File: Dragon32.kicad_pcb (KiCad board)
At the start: 2 copper layers, 120.2 x 78.9 mm, 59 parts, among them IC1 74LS273N, IC10 74LS32N, IC11 74LS123N, IC12 LM1889N, IC13 2318, IC15 MC14053, IC2 MC6847, IC3 74LS00N, IC4 74LS20N, IC5 74LS86AN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

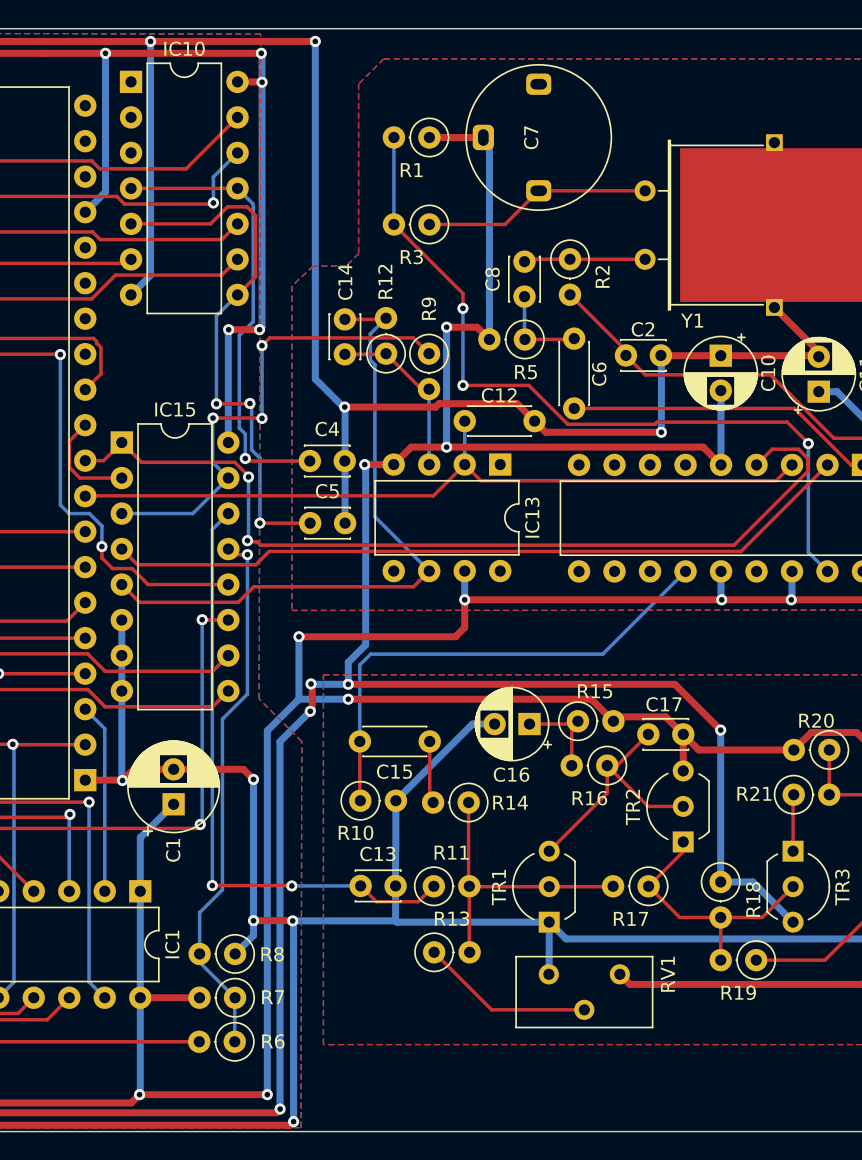
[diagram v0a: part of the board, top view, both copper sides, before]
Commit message: fix diff amp wiring
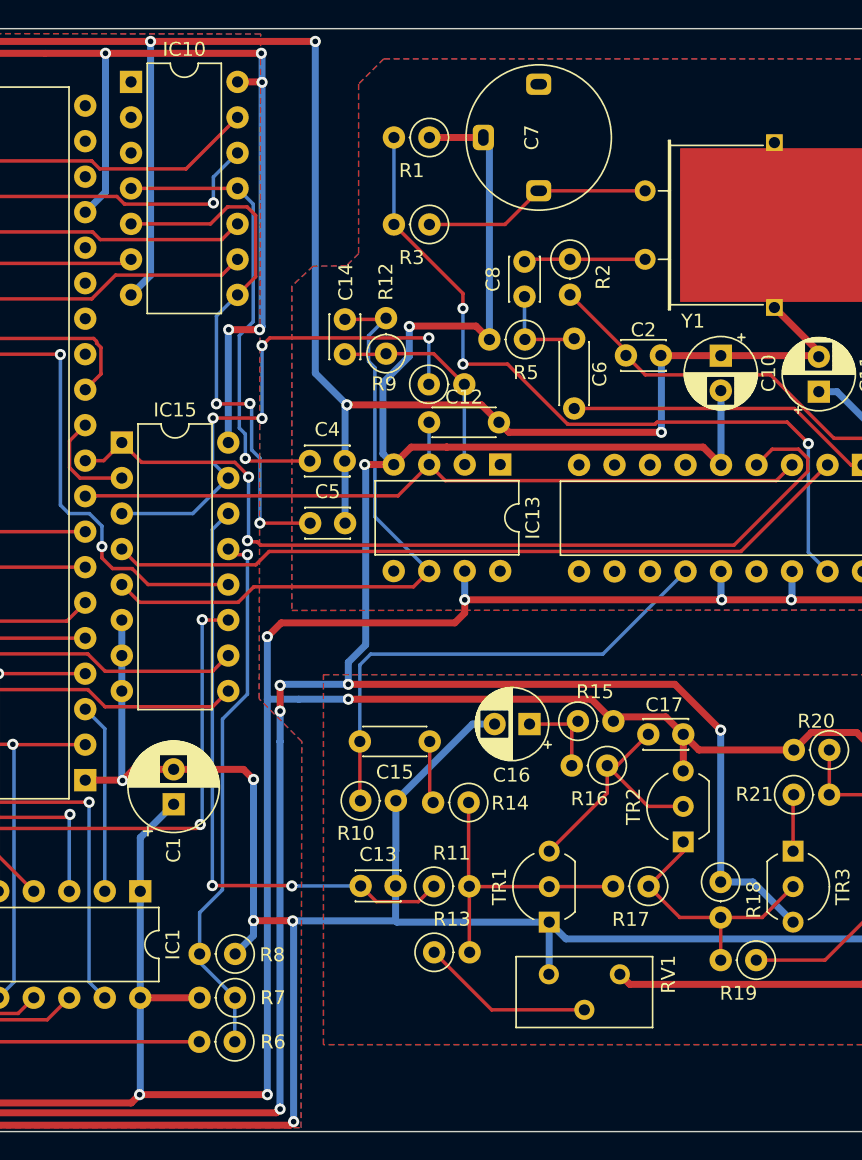
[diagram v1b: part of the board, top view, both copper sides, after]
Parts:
- moved C12 2.55 mm to (317.1, 78.5)
- moved R9 2.20 mm to (317.1, 75.7), turned to 0 degrees
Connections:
- C14 pad 1: Net-(IC13-+) -> Net-(IC13--)
- IC13 pad 2: CHB -> Net-(IC13--)
- IC13 pad 3: Net-(IC13-+) -> CHB
- R12 pad 1: Net-(IC13-+) -> Net-(IC13--)
- R9 pad 2: Net-(IC13-+) -> Net-(IC13--)
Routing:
- net Net-(IC13--): track 0.00 -> 15.2 mm
- net Net-(IC13-+): track 12.5 -> 0.00 mm
- net -5V: track 261.8 -> 268.1 mm, vias 10 -> 9
- net +5V: track 592.7 -> 595.6 mm
- net MUX Y: track 34.8 -> 37.7 mm, vias 3 -> 4
- net ChrOSC: track 56.1 -> 55.2 mm

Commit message: notch edge of board for clearance of relay
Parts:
- moved R20 138.4 mm to (207.6, 110.1), turned to 90 degrees
- moved R1 137.3 mm to (180.0, 64.8)
- moved C7 137.3 mm to (187.9, 64.8)
- moved R3 137.2 mm to (180.0, 68.6)
- moved C16 136.5 mm to (187.9, 105.7), turned to -90 degrees
- moved R13 135.4 mm to (182.6, 127.7)
- moved R19 135.3 mm to (205.6, 127.3)
- moved R14 135.2 mm to (185.0, 114.8)
- moved C15 135.2 mm to (182.2, 110.5)
- moved R10 135.2 mm to (177.3, 114.7)
- moved R18 135.2 mm to (203.0, 120.2)
- moved TR3 135.2 mm to (208.2, 118.0)
- moved R17 135.2 mm to (197.9, 120.5)
- moved RV1 135.2 mm to (195.9, 127.4)
- moved C17 135.1 mm to (200.4, 108.4)
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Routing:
- net GND: track 642.0 -> 572.8 mm
- net +5V: track 595.6 -> 609.4 mm
- net MUX Y: track 37.7 -> 43.1 mm
- net Net-(TR1-C): track 18.4 -> 23.4 mm
- net VID OUT: track 10.8 -> 15.6 mm
- net Composite: track 35.8 -> 40.0 mm
- net Net-(TR2-E): track 19.4 -> 22.6 mm
- net MUX X: track 43.9 -> 46.4 mm
- net Net-(TR3-E): track 4.06 -> 6.37 mm
- net Net-(C16-Pad1): track 6.91 -> 8.99 mm
- net Net-(TR1-B): track 21.1 -> 23.1 mm
- net Net-(C7-Pad1): track 16.4 -> 18.1 mm
- net -5V: track 268.1 -> 268.9 mm
- net Net-(R13-Pad1): track 12.5 -> 11.7 mm
- net GM2: track 90.5 -> 89.8 mm
- removed copper zone on B.Cu, net (none)
- removed copper zone on F.Cu, net (none)
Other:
- outline, holes or cut-outs redrawn

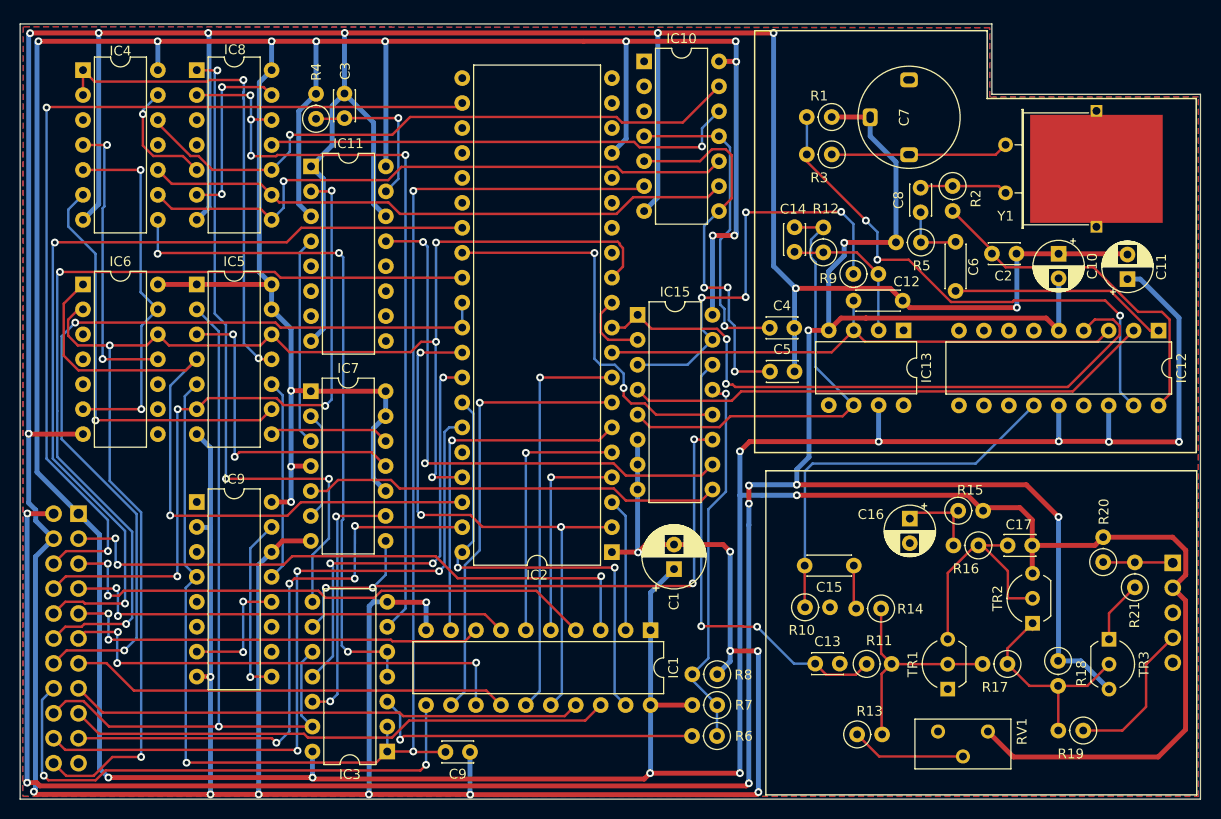
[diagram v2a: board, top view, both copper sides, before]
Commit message: move -5v
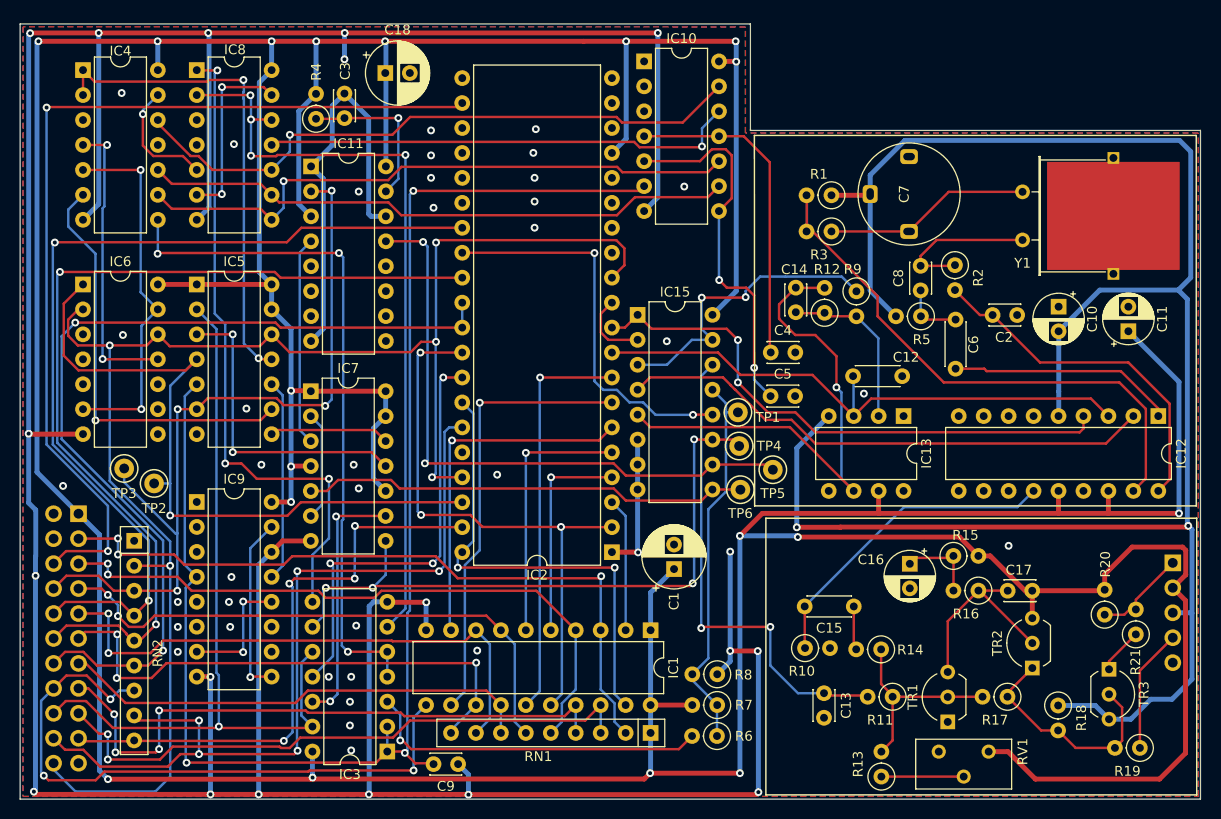
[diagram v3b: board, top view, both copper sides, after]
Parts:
- added C18: 100uF, Capacitor_THT:CP_Radial_D6.3mm_P2.50mm, F.Cu at (134.5, 60.3)
- added RN1: 4K7, Resistor_THT:R_Array_SIP9, F.Cu at (161.5, 127.5)
- added RN2: 4K7, Resistor_THT:R_Array_SIP9, F.Cu at (109.0, 108.0)
- added TP1: TestPoint_LinePulse, TestPoint:TestPoint_Keystone_5000-5004_Miniature, F.Cu at (170.4, 94.9)
- added TP2: TestPoint_HS, TestPoint:TestPoint_Keystone_5000-5004_Miniature, F.Cu at (111.0, 102.1)
- added TP3: TestPoint_NHS, TestPoint:TestPoint_Keystone_5000-5004_Miniature, F.Cu at (108.0, 100.6)
- added TP4: TestPoint_NHS, TestPoint:TestPoint_Keystone_5000-5004_Miniature, F.Cu at (170.6, 98.3)
- added TP5: TestPoint_NHS, TestPoint:TestPoint_Keystone_5000-5004_Miniature, F.Cu at (174.0, 100.7)
- added TP6: TestPoint_NHS, TestPoint:TestPoint_Keystone_5000-5004_Miniature, F.Cu at (170.7, 102.7)
- moved IC13 8.73 mm to (187.3, 95.2)
- moved IC12 8.70 mm to (213.2, 95.2)
- moved R2 8.06 mm to (192.5, 79.9)
- moved R1 7.97 mm to (180.0, 72.8)
- moved C8 7.95 mm to (189.0, 82.5)
- moved C6 7.92 mm to (192.6, 85.4)
- moved R3 7.84 mm to (180.0, 76.5)
- moved C7 7.81 mm to (187.9, 72.6)
- moved C12 7.69 mm to (182.2, 91.2)
- moved R5 7.52 mm to (189.1, 85.1)
- moved C2 6.25 mm to (196.4, 85.0)
- moved C14 6.15 mm to (176.3, 84.7)
- moved R12 6.15 mm to (179.3, 84.7)
- moved R19 6.03 mm to (211.4, 129.0)
- moved C10 5.39 mm to (203.1, 84.1)
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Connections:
- net /LINE PULSES renamed /HS LINE PULSES
- net Net-(IC1-Q0) renamed /D0
- net Net-(IC1-Q1) renamed /D1
- net Net-(IC1-Q2) renamed /D2
- net Net-(IC1-Q3) renamed /D3
- net Net-(IC1-Q4) renamed /D4
- net Net-(IC1-Q5) renamed /D5
- net Net-(IC1-Q6) renamed /D6
- net Net-(IC1-Q7) renamed /D7
- IC3 pad 8: /~{VCLK} -> /VCLK'
- IC5 pad 3: Net-(IC7B-C) -> /~{VCLK}
- IC7 pad 11: Net-(IC7B-C) -> /~{VCLK}
- IC8 pad 1: /~{VCLK} -> /VCLK'
- J1 pad 2: -5V -> unconnected-(J1-Pin_2-Pad2)
- J2 pad 3: unconnected-(J2-Pin_3-Pad3) -> -5V
- R11 pad 1: MUX X -> Net-(TR1-B)
- R11 pad 2: Net-(TR1-B) -> MUX X
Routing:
- net GND: track 572.8 -> 443.9 mm, vias 21 -> 56
- net /VCLK': track 0.00 -> 67.1 mm, vias 0 -> 3
- net -5V: track 268.9 -> 202.0 mm, vias 9 -> 2
- net /~{VCLK}: track 68.0 -> 31.8 mm, vias 3 -> 2
- net Net-(IC7B-C): track 32.4 -> 0.00 mm, vias 2 -> 0
- net DO3: track 43.7 -> 57.1 mm
- net MUX Y: track 43.1 -> 31.1 mm, vias 4 -> 2
- net DO2: track 46.5 -> 58.6 mm
- net ~{A}/G: track 74.5 -> 86.1 mm, vias 3 -> 5
- net ~{NHS}: track 70.3 -> 81.4 mm
- net ~{FS}: track 147.5 -> 158.6 mm
- net DO0: track 62.7 -> 73.7 mm
- net DO6: track 52.3 -> 63.1 mm, vias 0 -> 4
- net +5V: track 609.4 -> 599.6 mm, vias 23 -> 18
- net DO1: track 56.4 -> 66.2 mm
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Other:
- outline, holes or cut-outs redrawn

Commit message: trial ATF1504
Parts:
- removed C5: 100pF, Capacitor_THT:C_Disc_D3.0mm_W2.0mm_P2.50mm
- removed C9: 180pF, Capacitor_THT:C_Disc_D3.0mm_W2.0mm_P2.50mm
- removed IC10: 74LS32N, Package_DIP:DIP-14_W7.62mm
- removed IC3: 74LS00N, Package_DIP:DIP-14_W7.62mm
- removed IC4: 74LS20N, Package_DIP:DIP-14_W7.62mm
- removed IC5: 74LS86AN, Package_DIP:DIP-14_W7.62mm
- removed IC6, IC8: 74LS393N, Package_DIP:DIP-14_W7.62mm
- removed IC7: 74ALS74N, Package_DIP:DIP-14_W7.62mm
- removed IC9: 74LS390, Package_DIP:DIP-16_W7.62mm
- added U1: ATF1504ASL-xAx44, Package_QFP:TQFP-44_10x10mm_P0.8mm, F.Cu at (110.9, 70.8)
- C4: value 180pF -> 0.01uF; footprint Capacitor_THT:C_Disc_D3.0mm_W2.0mm_P2.50mm -> Capacitor_THT:C_Disc_D4.3mm_W1.9mm_P5.00mm
- R6: value 12K -> 1K8
- R8: value 1K8 -> 12K
- moved R6 2.57 mm to (165.7, 127.8), turned to 0 degrees
- moved R8 2.52 mm to (165.8, 121.6), turned to 0 degrees
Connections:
- C4 pad 1: Net-(C4-Pad1) -> +5V
- IC11 pad 10: unconnected-(IC11B-B-Pad10) -> +5V
- IC11 pad 11: unconnected-(IC11B-Clr-Pad11) -> GND
- IC11 pad 2: ~{NHS} -> Burst
- IC11 pad 4: Net-(IC11A-~{Q}) -> PhaseT
- IC11 pad 6: unconnected-(IC11B-Cext-Pad6) -> GND
- IC11 pad 9: unconnected-(IC11B-A-Pad9) -> GND
- IC2 pad 22: DA0 -> DA0'
- J1 pad 21: unconnected-(J1-Pin_21-Pad21) -> E
- R6 pad 1: LINE PULSE -> GND
- R6 pad 2: Net-(IC3-Pad3) -> LINE PULSE
- R8 pad 1: GND -> PadLuma
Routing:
- net GND: track 443.9 -> 14.3 mm, vias 56 -> 32
- net /HS LINE PULSES: track 150.0 -> 0.00 mm, vias 3 -> 0
- net PadLuma: track 0.00 -> 105.4 mm, vias 0 -> 2
- net Net-(IC8A-MR): track 78.4 -> 0.00 mm, vias 4 -> 0
- net Net-(IC3-Pad4): track 69.6 -> 0.00 mm, vias 3 -> 0
- net /VCLK': track 67.1 -> 0.00 mm, vias 3 -> 0
- net E: track 0.00 -> 66.2 mm
- net Net-(IC8B-Q1): track 64.4 -> 0.00 mm, vias 1 -> 0
- net Net-(IC8B-Q3): track 62.7 -> 0.00 mm, vias 1 -> 0
- net Net-(IC8B-Q2): track 60.3 -> 0.00 mm
- net DA0': track 0.00 -> 50.9 mm, vias 0 -> 2
- net LUM CONTROL: track 67.0 -> 117.7 mm
- net Net-(IC4-Pad1): track 49.8 -> 0.00 mm, vias 2 -> 0
- net Net-(IC8B-Q0): track 48.6 -> 0.00 mm, vias 1 -> 0
- net +5V: track 599.6 -> 553.9 mm, vias 18 -> 17
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
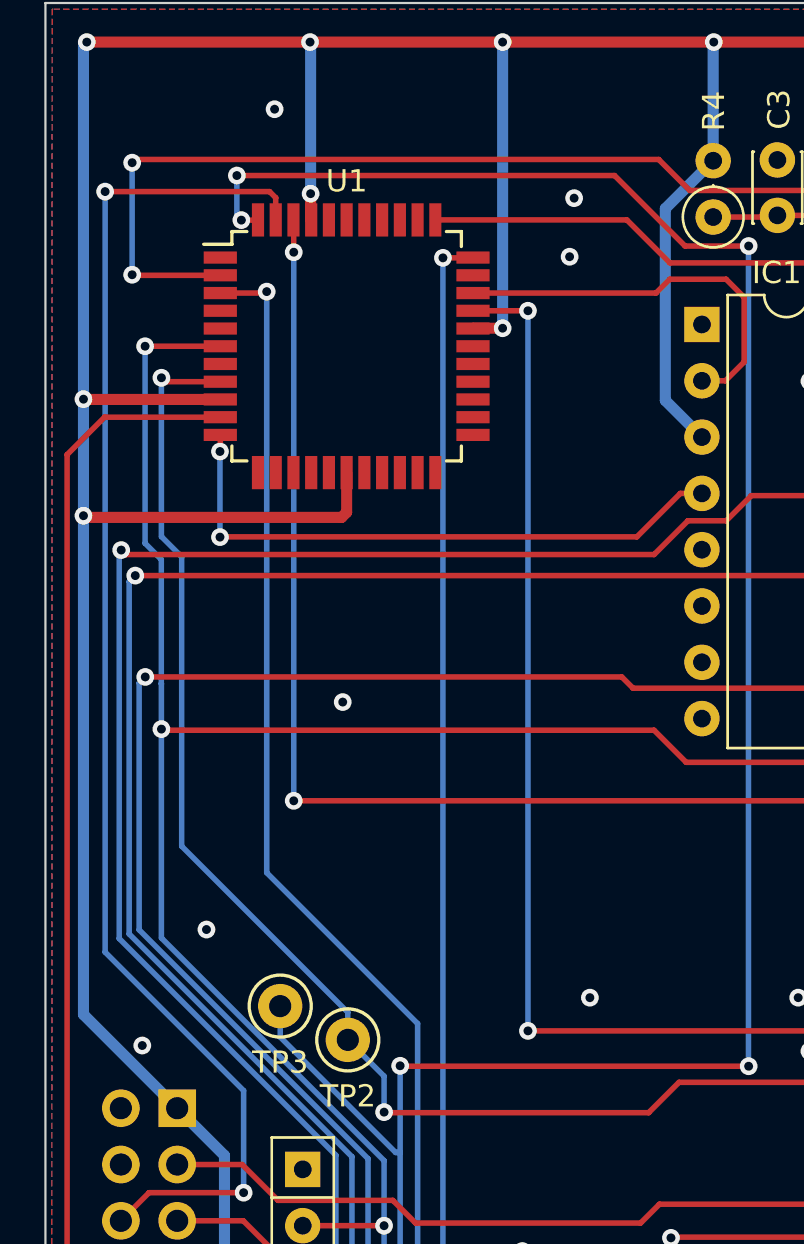
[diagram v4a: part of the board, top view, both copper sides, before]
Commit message: provide jtag connections
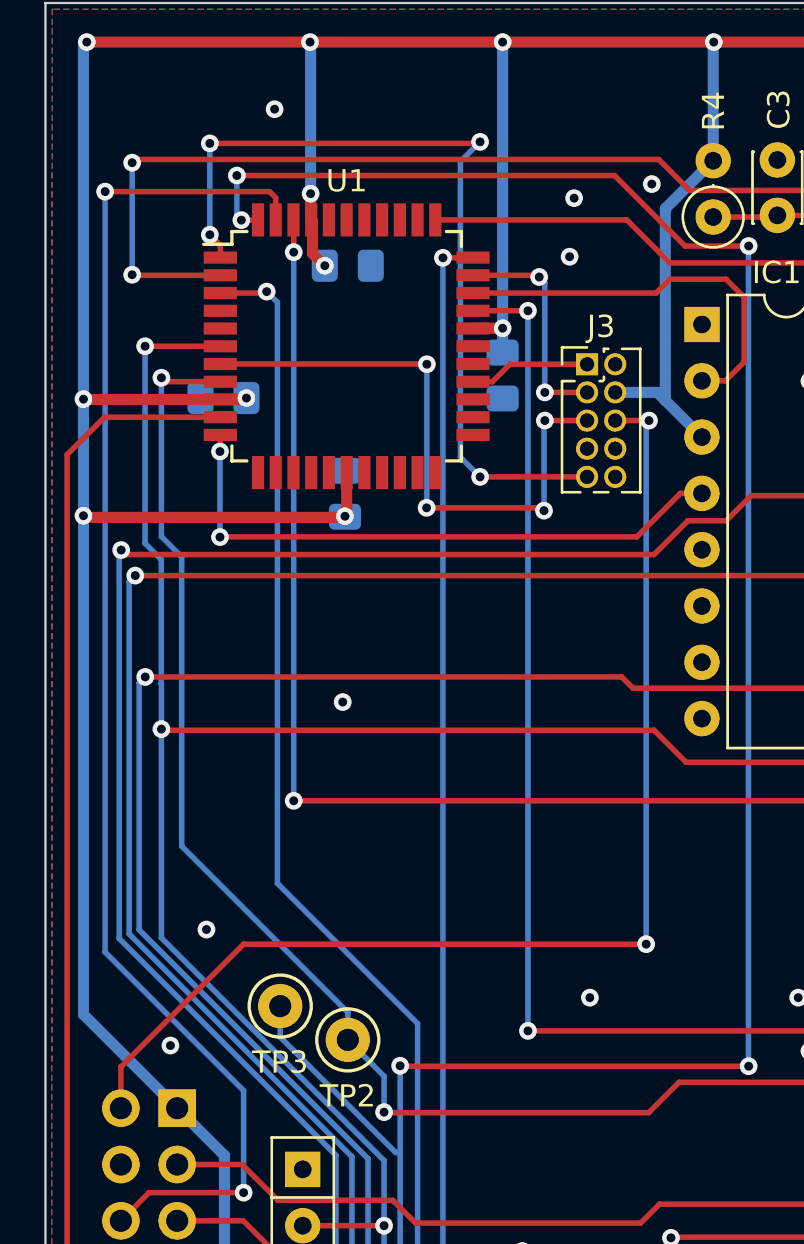
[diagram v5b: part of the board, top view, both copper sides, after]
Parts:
- added C19: 0.1uF, Capacitor_SMD:C_0805_2012Metric_Pad1.18x1.45mm_HandSolder, B.Cu at (105.4, 73.2)
- added C20: 0.1uF, Capacitor_SMD:C_0805_2012Metric_Pad1.18x1.45mm_HandSolder, B.Cu at (111.0, 67.2)
- added C5: 0.1uF, Capacitor_SMD:C_0805_2012Metric_Pad1.18x1.45mm_HandSolder, B.Cu at (110.9, 77.5)
- added C9: 0.1uF, Capacitor_SMD:C_0805_2012Metric_Pad1.18x1.45mm_HandSolder, B.Cu at (118.0, 72.1)
- added J3: JTAG, Connector_PinHeader_1.27mm:PinHeader_2x05_P1.27mm_Vertical, F.Cu at (121.8, 71.6)
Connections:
- J1 pad 2: unconnected-(J1-Pin_2-Pad2) -> ~{RESET}
- U1 pad 7: unconnected-(U1-I/O/TMS-Pad7) -> TMS
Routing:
- net ~{RESET}: track 0.00 -> 53.1 mm, vias 0 -> 2
- net TDI: track 0.00 -> 38.2 mm, vias 0 -> 4
- net TMS: track 0.00 -> 27.1 mm, vias 0 -> 4
- net TDO: track 0.00 -> 10.2 mm, vias 0 -> 2
- net +5V: track 553.9 -> 561.0 mm, vias 17 -> 20
- net TCK: track 0.00 -> 5.47 mm
- net GND: vias 32 -> 33

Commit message: revise layout
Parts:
- added TP7: TestPoint_Y, TestPoint:TestPoint_Keystone_5000-5004_Miniature, F.Cu at (175.8, 127.2)
- added TP8: TestPoint_C, TestPoint:TestPoint_Keystone_5000-5004_Miniature, F.Cu at (177.2, 111.4)
- moved C18 49.3 mm to (110.4, 103.3), turned to 90 degrees
- moved R8 48.2 mm to (161.4, 73.6)
- moved R6 48.2 mm to (161.3, 79.9)
- moved R7 48.2 mm to (163.9, 76.7)
- moved TP3 29.1 mm to (112.3, 71.8)
- moved TP2 29.1 mm to (128.7, 79.0)
- moved IC11 28.8 mm to (114.8, 96.0), turned to 90 degrees
- moved C19 28.6 mm to (133.2, 79.8)
- moved C20 28.6 mm to (138.8, 73.8)
- moved U1 28.6 mm to (138.8, 77.4)
- moved C5 28.1 mm to (138.8, 80.8)
- moved J3 28.0 mm to (149.6, 74.6)
- moved C9 25.7 mm to (143.1, 77.7)
- moved C3 24.2 mm to (117.3, 85.3)
- moved R4 24.0 mm to (114.5, 85.2)
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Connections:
- RN2 pad 2: ~{FS} -> ~{NHS}
- RN2 pad 3: ~{NHS} -> GM2
- RN2 pad 4: GM2 -> GM1
- RN2 pad 5: GM1 -> GM0
- RN2 pad 6: GM0 -> ~{RAS0}
- RN2 pad 7: ~{RAS0} -> ~{A}/G
- RN2 pad 8: ~{A}/G -> CSS
- RN2 pad 9: CSS -> ~{FS}
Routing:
- net +5V: track 561.0 -> 6.36 mm, vias 20 -> 4
- net PadLuma: track 105.4 -> 21.3 mm, vias 2 -> 0
- net LUM CONTROL: track 117.7 -> 35.4 mm, vias 4 -> 1
- net CHROME CONTROL: track 88.3 -> 27.0 mm, vias 2 -> 0
- net GM2: track 92.9 -> 32.9 mm, vias 2 -> 0
- net ~{FS}: track 175.6 -> 116.9 mm, vias 6 -> 3
- net GM1: track 92.8 -> 37.3 mm, vias 2 -> 0
- net GM0: track 93.9 -> 42.7 mm, vias 2 -> 0
- net ~{RESET}: track 53.1 -> 99.0 mm, vias 2 -> 3
- net MUX X: track 49.5 -> 95.3 mm, vias 2 -> 0
- net ~{NHS}: track 112.5 -> 72.3 mm, vias 6 -> 1
- net CHB: track 58.8 -> 93.2 mm
- net MUX Y: track 31.1 -> 59.8 mm, vias 2 -> 1
- net E: track 66.2 -> 90.5 mm, vias 0 -> 1
- net Burst: track 18.0 -> 42.3 mm, vias 0 -> 1
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- added copper zone on In1.Cu, net +5V
- added copper zone on In2.Cu, net GND
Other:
- board size 120.2 x 78.9 mm -> 120.2 x 66.9 mm
- copper layers 2 -> 4
